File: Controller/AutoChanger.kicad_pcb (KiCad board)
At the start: 2 copper layers, 130.1 x 32 mm, 40 parts, among them P1 CONNECT, P10 SENSOR, P11 SENSOR, P12 LOGO, P13 5, P3 1, P4 2, P5 3, P6 4, P7 6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

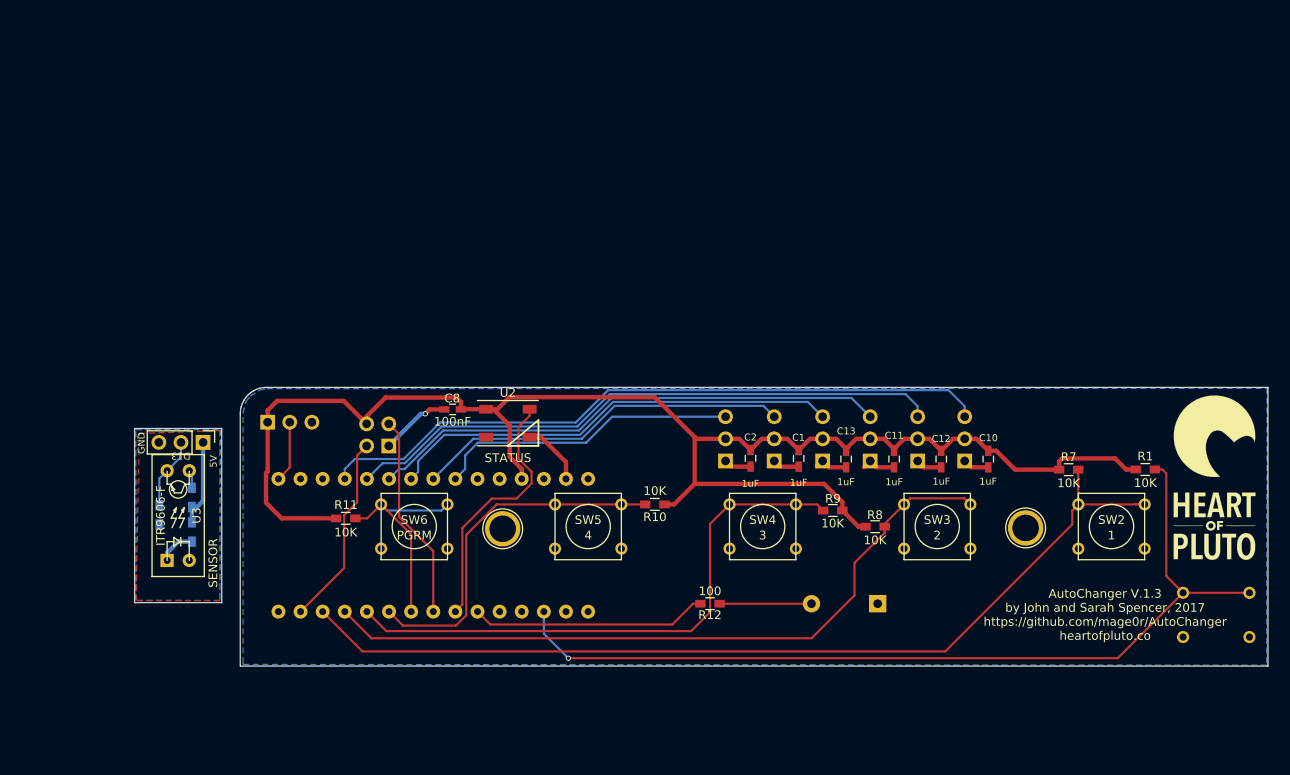
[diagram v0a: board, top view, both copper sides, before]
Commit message: Added basic OLED stuff
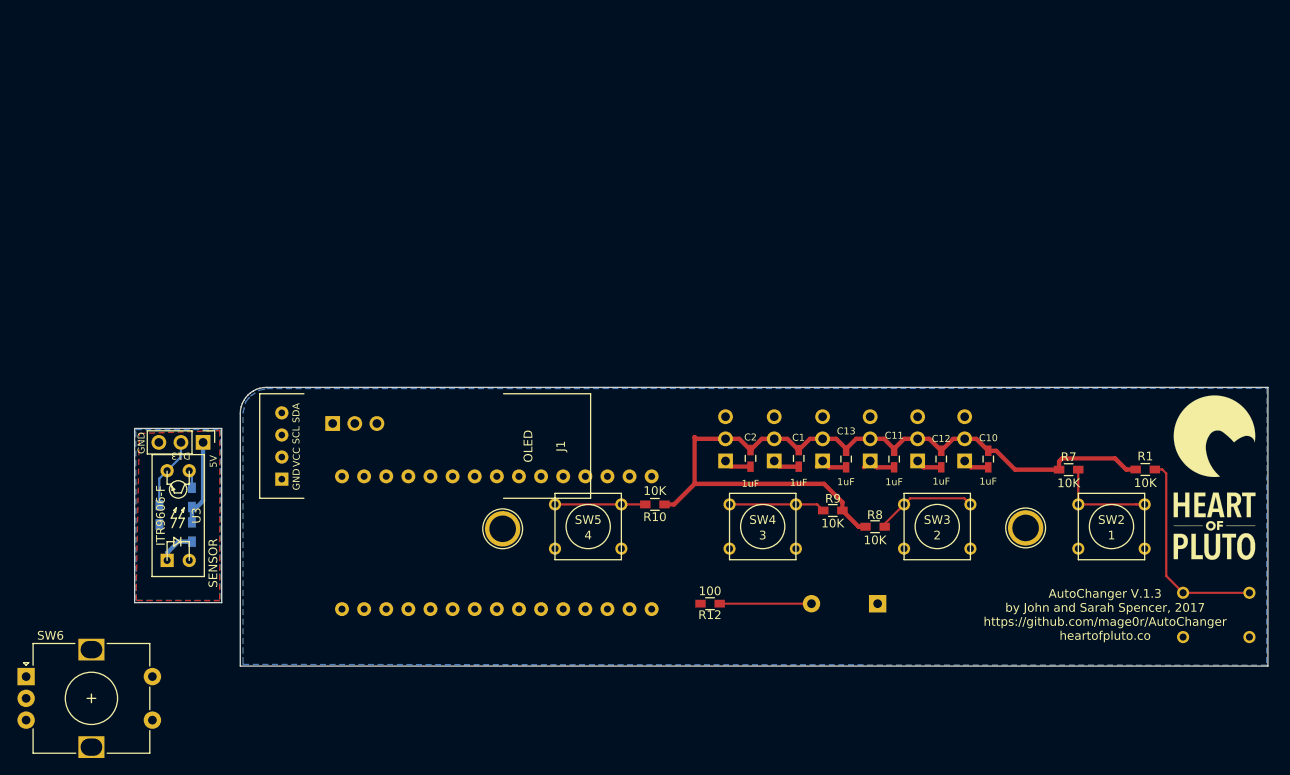
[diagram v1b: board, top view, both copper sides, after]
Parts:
- removed C8: 100nF, Capacitors_SMD:C_0603_HandSoldering
- removed P1: CONNECT, Pin_Headers:Pin_Header_Straight_2x02_Pitch2.54mm
- removed R11: 10K, Resistors_SMD:R_0603_HandSoldering
- removed U2: STATUS, LEDs:LED_WS2812B-PLCC4
- added J1: OLED, libs:0.91 OLED, F.Cu at (110.4, 86.8)
- SW6: value PGRM -> PRGM; footprint Buttons_Switches_ThroughHole:SW_PUSH_SMALL -> Rotary_Encoder:RotaryEncoder_Alps_EC12E-Switch_Vertical_H20mm
- moved SW6 47.8 mm to (64.6, 113.3)
- moved P10 7.47 mm to (99.8, 84.2)
- moved U1 7.31 mm to (118.7, 97.9)
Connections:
- P13 pad 3: /A4 -> /A7
- P7 pad 3: /A5 -> /A6
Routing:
- net /D10: track 108.2 -> 11.6 mm
- net +5V: track 188.2 -> 102.4 mm
- net /RESET: track 103.8 -> 23.6 mm, vias 1 -> 0
- net /A0: track 78.0 -> 0.00 mm
- net /D9: track 82.8 -> 11.7 mm
- net /A1: track 69.1 -> 0.00 mm
- net /A2: track 60.0 -> 0.00 mm
- net /D8: track 66.0 -> 11.5 mm
- net /A3: track 52.3 -> 0.00 mm
- net /A4: track 43.1 -> 0.00 mm
- net /A5: track 34.9 -> 0.00 mm
- net /D7: track 41.3 -> 10.4 mm
- net /D4: track 29.7 -> 0.00 mm
- net /D3: track 27.2 -> 0.00 mm
- net /D6: track 26.1 -> 0.00 mm
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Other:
- board text removed: "RX D11"
- board text removed: "TX D5"

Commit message: Tinypico compatible controller
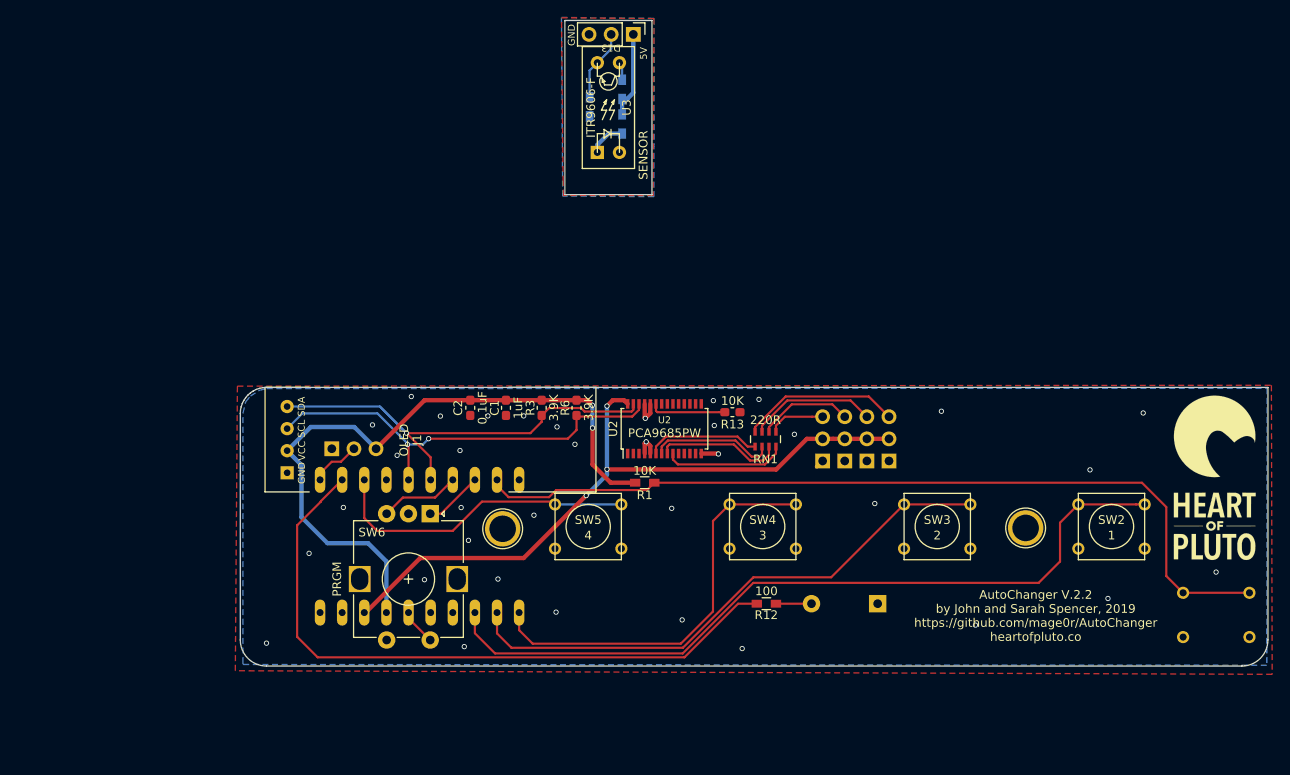
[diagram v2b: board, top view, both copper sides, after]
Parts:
- removed C10, C11, C12, C13: 1uF, Capacitors_SMD:C_0603_HandSoldering
- removed P13: 5, Pin_Headers:Pin_Header_Straight_1x03_Pitch2.54mm
- removed P7: 6, Pin_Headers:Pin_Header_Straight_1x03_Pitch2.54mm
- removed R10, R7, R8, R9: 10K, Resistors_SMD:R_0603_HandSoldering
- added R13: 10K, Resistor_SMD:R_0603_1608Metric_Pad1.05x0.95mm_HandSolder, F.Cu at (145.7, 82.9)
- added R3: 3.9K, Resistor_SMD:R_0603_1608Metric_Pad1.05x0.95mm_HandSolder, F.Cu at (123.8, 82.4)
- added R6: 3.9K, Resistor_SMD:R_0603_1608Metric_Pad1.05x0.95mm_HandSolder, F.Cu at (127.8, 82.4)
- added RN1: 220R, Resistor_SMD:R_Array_Concave_4x0603, F.Cu at (149.5, 86.0)
- added U2: PCA9685PW, Package_SO:TSSOP-28_4.4x9.7mm_P0.65mm, F.Cu at (137.9, 84.8)
- C1: footprint Capacitors_SMD:C_0603_HandSoldering -> Capacitor_SMD:C_0603_1608Metric_Pad1.05x0.95mm_HandSolder
- C2: value 1uF -> 0.1uF; footprint Capacitors_SMD:C_0603_HandSoldering -> Capacitor_SMD:C_0603_1608Metric_Pad1.05x0.95mm_HandSolder
- U1: value arduino_nano -> TinyPico; footprint arduino:nano -> libs:TinyPico
- moved R5 68.1 mm to (129.3, 47.8)
- moved P11 68.1 mm to (134.3, 39.5)
- moved R2 68.1 mm to (133.0, 45.8)
- moved R4 68.1 mm to (133.0, 49.8)
- moved U3 68.1 mm to (131.5, 47.9)
- moved R1 57.5 mm to (135.6, 91.0)
- moved SW6 50.0 mm to (111.0, 94.6), turned to 270 degrees
- moved C1 34.1 mm to (119.7, 82.4), turned to 270 degrees
- moved C2 32.7 mm to (115.6, 82.4), turned to 270 degrees
- moved U1 8.88 mm to (109.8, 98.3), turned to 180 degrees
- moved P3 8.69 mm to (163.7, 88.5)
- moved R12 6.47 mm to (149.6, 104.9)
- moved P4 5.83 mm to (161.1, 88.5)
- moved P5 2.92 mm to (158.6, 88.5)
- moved P10 2.90 mm to (99.7, 87.1)
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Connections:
- C1 pad 1: GND -> +3V3
- C1 pad 2: +5V -> GND
- C2 pad 1: GND -> +3V3
- C2 pad 2: +5V -> GND
- J1 pad 2: +5V -> +3V3
- J1 pad 3: /A5 -> /SCL
- J1 pad 4: /A4 -> /SDA
- P10 pad 1: +5V -> GND
- P10 pad 2: /D13 -> /GPIO23
- P10 pad 3: GND -> +3V3
- P11 pad 1: +5V -> /3V3_C
- P11 pad 2: /D13 -> /GPIO25_C
- P11 pad 3: GND -> /GND_C
- P3 pad 3: /A0 -> /PWM0
- P4 pad 3: /A1 -> /PWM1
- P5 pad 3: /A2 -> /PWM2
- P6 pad 3: /A3 -> /PWM3
- R1 pad 1: +5V -> +3V3
- R12 pad 1: /D3 -> /GPIO19
- R2 pad 1: +5V -> /3V3_C
- R4 pad 1: +5V -> /3V3_C
- R5 pad 1: /D13 -> /GPIO25_C
- R5 pad 2: GND -> /GND_C
- SW2 pad 1: /D10 -> /GPIO27
- SW3 pad 1: /D9 -> /GPIO26
- SW4 pad 1: /D8 -> /GPIO25
- SW5 pad 1: /D7 -> /GPIO18
- SW6 pad A: /D11 -> /GPIO33
- SW6 pad B: /D12 -> /GPIO32
- SW6 pad S1: /D6 -> /GPIO4
- U1 pad 1: /D13 -> /GPIO25
- U1 pad 10: /A6 -> Net-(U1-Pad10)
- U1 pad 11: /A7 -> /GPIO23
- U1 pad 12: +5V -> /GPIO19
- U1 pad 13: /RESET -> /GPIO18
- U1 pad 14: GND -> /GPIO5
- U1 pad 15: /VIN -> /SCL
- U1 pad 16: /TXD -> /SDA
- U1 pad 17: /RXD -> /GPIO32
- U1 pad 18: /RESET -> /GPIO33
- U1 pad 19: GND -> /RESET
- U1 pad 2: /3V3 -> /GPIO26
- U1 pad 20: /D2 -> GND
- U1 pad 3: /AREF -> /GPIO27
- U1 pad 4: /A0 -> /GPIO15
- U1 pad 5: /A1 -> /GPIO14
- U1 pad 6: /A2 -> /GPIO4
- U1 pad 7: /A3 -> +3V3
- U1 pad 8: /A4 -> +5V
- U1 pad 9: /A5 -> GND
- U3 pad 2: GND -> /GND_C
- U3 pad 4: /D13 -> /GPIO25_C
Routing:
- net /GPIO27: track 0.00 -> 89.9 mm
- net +3V3: track 0.00 -> 78.4 mm, vias 0 -> 2
- net /GPIO19: track 0.00 -> 76.5 mm
- net /RESET: track 23.6 -> 98.2 mm
- net /GPIO26: track 0.00 -> 64.3 mm
- net /SDA: track 0.00 -> 54.3 mm, vias 0 -> 1
- net /SCL: track 0.00 -> 50.2 mm, vias 0 -> 2
- net /GPIO25: track 0.00 -> 47.6 mm
- net /GPIO18: track 0.00 -> 36.1 mm
- net +5V: track 102.4 -> 79.4 mm, vias 0 -> 3
- net /PWM0: track 0.00 -> 18.3 mm
- net /PWM1: track 0.00 -> 14.7 mm
- net Net-(RN1-Pad3): track 0.00 -> 14.6 mm
- net Net-(RN1-Pad2): track 0.00 -> 14.3 mm
- net Net-(RN1-Pad4): track 0.00 -> 14.1 mm
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- added copper zone on B.Cu, net /GND_C
- added copper zone on F.Cu, net /GND_C
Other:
- board size 130.1 x 32 mm -> 118 x 74.1 mm
- board text added: "+3V3"
- board text added: "AutoChanger V.2.2 by John and Sarah Spencer, 2019 https://github.com/mage0r/AutoChanger heartofpluto.co"
- board text added: "D23"
- board text removed: "+5V"
- board text removed: "AutoChanger V.1.3 by John and Sarah Spencer, 2017 https://github.com/mage0r/AutoChanger heartofpluto.co"

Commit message: Updated for Kicad 7.0
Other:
- net class Default removed
